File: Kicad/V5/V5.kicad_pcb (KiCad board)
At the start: 2 copper layers, 88.9 x 119.4 mm, 40 parts, among them J1 Conn_01x02_Pin, J2 Conn_01x02_Pin, J3 Conn_01x02_Pin, J4 Conn_01x02_Pin, J5 Conn_01x02_Pin, J6 Conn_01x02_Pin, U1 ISOM8600DFGR, U10 ISOM8600DFGR, U11 ISOM8600DFGR, U12 ISOM8600DFGR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

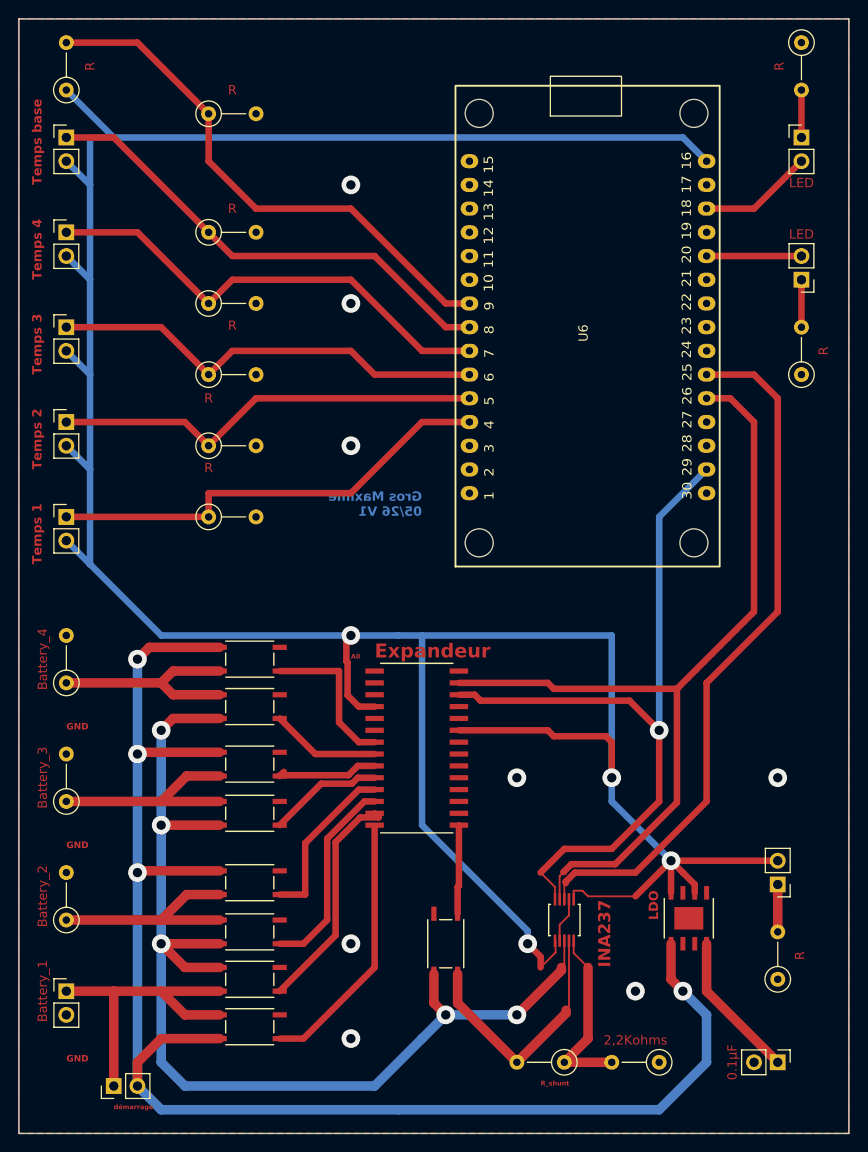
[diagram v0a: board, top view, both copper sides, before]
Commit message: ESP32 brownout à cause du bluetooth init
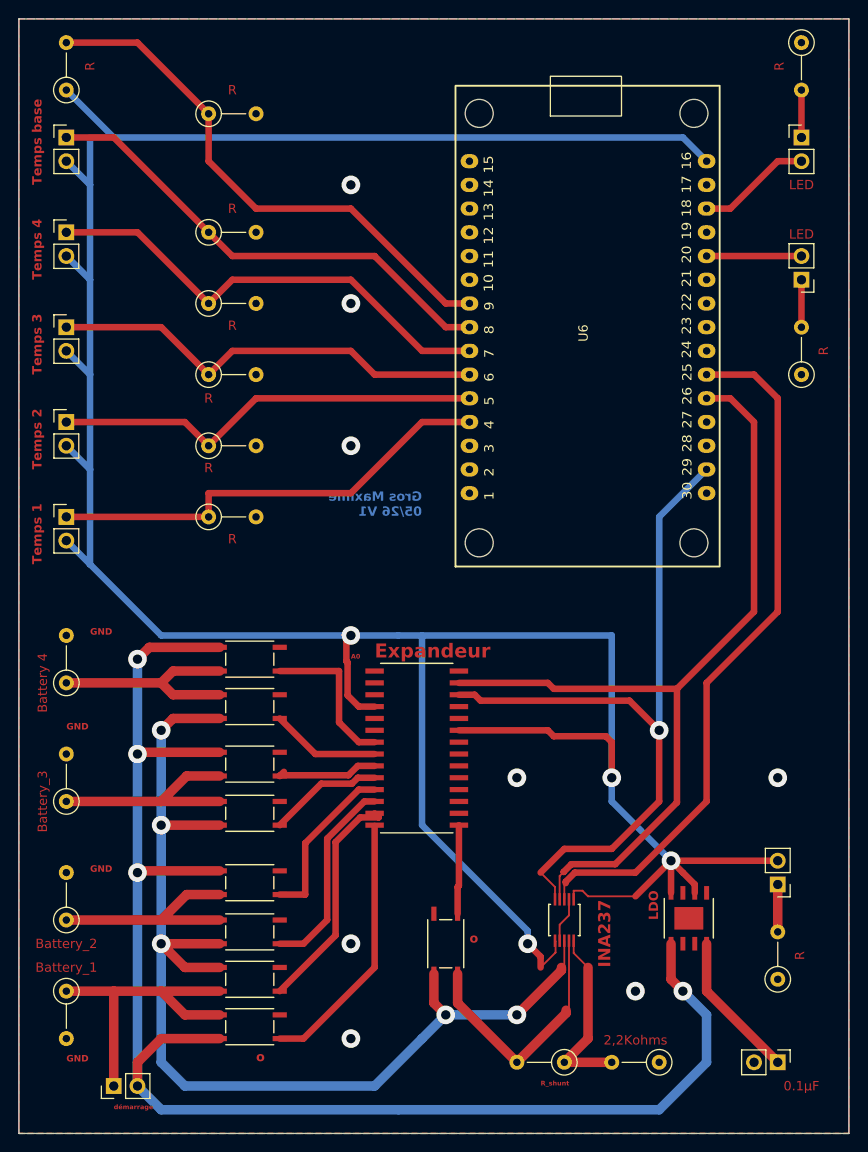
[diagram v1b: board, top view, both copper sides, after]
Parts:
- BT1: footprint Connector_PinHeader_2.54mm:PinHeader_1x02_P2.54mm_Vertical -> Resistor_THT:R_Axial_DIN0207_L6.3mm_D2.5mm_P5.08mm_Vertical
- BT4: value Battery_4 -> Battery 4
- turned BT1 to -90 degrees
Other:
- board text added: "o"
